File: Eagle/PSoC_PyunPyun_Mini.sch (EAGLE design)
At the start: 26 parts, among them IC1 NJM2732

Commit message: change Bord Design
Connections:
- net IDAC7: now also JP3.9; no longer JP3.8
- net IDAC8: now also JP3.8; no longer JP3.9
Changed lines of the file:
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@@
 <net name="IDAC8" class="0">
 <segment>
-<pinref part="JP3" gate="A" pin="9"/>
-<wire x1="101.6" y1="111.76" x2="114.3" y2="111.76" width="0.1524" layer="91"/>
-<wire x1="114.3" y1="111.76" x2="114.3" y2="86.36" width="0.1524" layer="91"/>
+<wire x1="114.3" y1="114.3" x2="114.3" y2="86.36" width="0.1524" layer="91"/>
 <wire x1="114.3" y1="86.36" x2="30.48" y2="86.36" width="0.1524" layer="91"/>
-<label x="106.68" y="111.76" size="1.778" layer="95"/>
 <pinref part="R5" gate="G$1" pin="1"/>
 <wire x1="30.48" y1="68.58" x2="35.56" y2="68.58" width="0.1524" layer="91"/>
@@
 <wire x1="30.48" y1="86.36" x2="30.48" y2="68.58" width="0.1524" layer="91"/>
 <junction x="30.48" y="68.58"/>
+<pinref part="JP3" gate="A" pin="8"/>
+<wire x1="101.6" y1="114.3" x2="114.3" y2="114.3" width="0.1524" layer="91"/>
+<label x="106.68" y="114.3" size="1.778" layer="95"/>
 </segment>
 </net>
@@
 <net name="IDAC7" class="0">
 <segment>
-<pinref part="JP3" gate="A" pin="8"/>
-<wire x1="101.6" y1="114.3" x2="114.3" y2="114.3" width="0.1524" layer="91"/>
-<label x="106.68" y="114.3" size="1.778" layer="95"/>
-</segment>
-</net>
+<pinref part="JP3" gate="A" pin="9"/>
+<wire x1="101.6" y1="111.76" x2="111.76" y2="111.76" width="0.1524" layer="91"/>
+<label x="106.68" y="111.76" size="1.778" layer="95"/>
+</segment>
+</net>

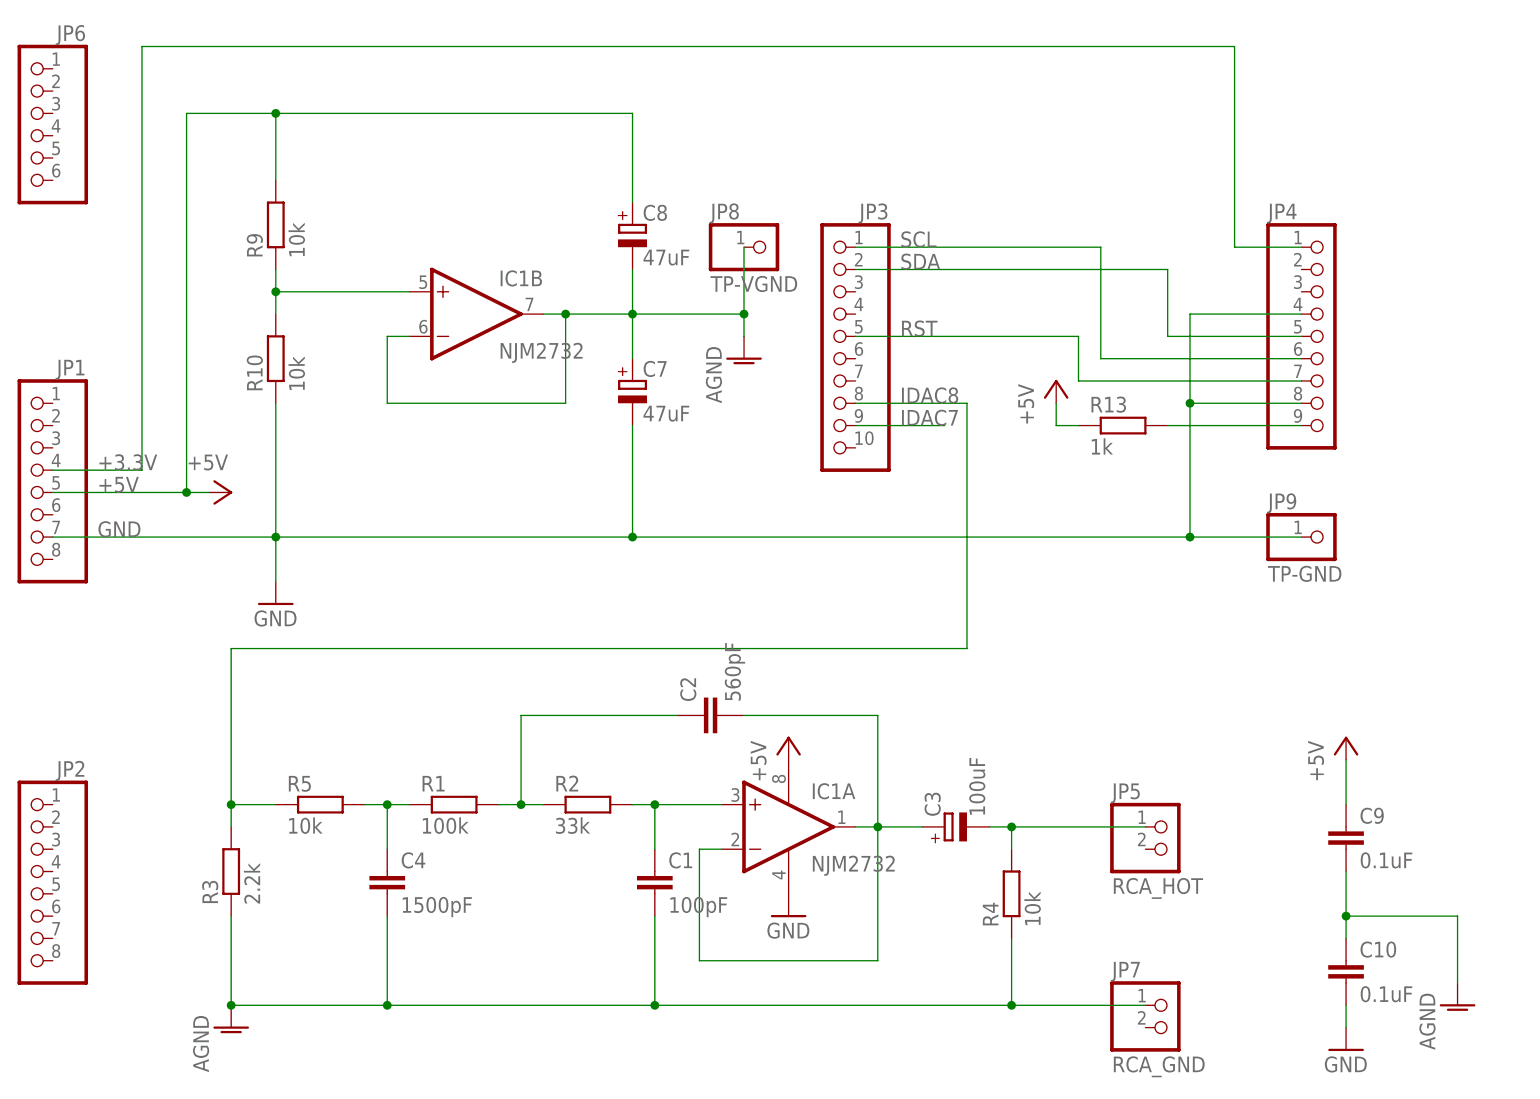
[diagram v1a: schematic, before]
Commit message: 回路図・基板図 RST信号に抵抗分圧を追加
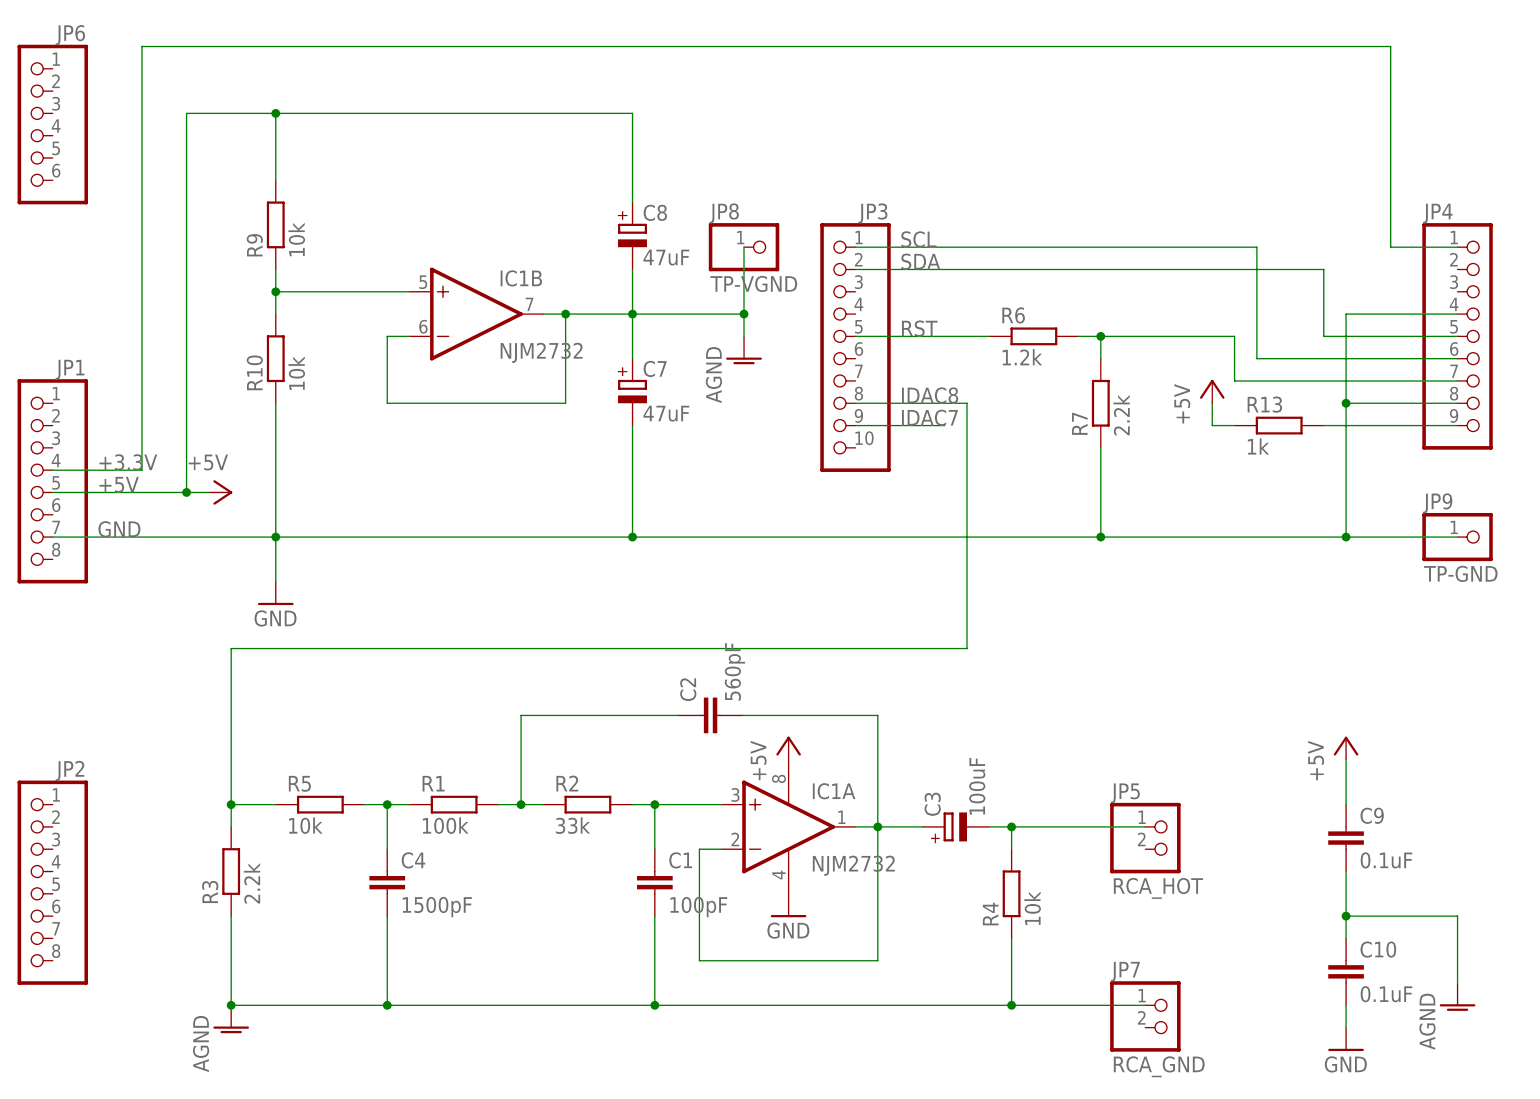
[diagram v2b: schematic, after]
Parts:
- added R6: 1.2k, rcl:R-EU_0207/7
- added R7: 2.2k, rcl:R-EU_0207/7
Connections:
- new net N$6: JP3.5, R6.1
- net GND: now also R7.1
- net RST: now also R6.2, R7.2; no longer JP3.5
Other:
- moved on the sheet: JP4, JP9, R13
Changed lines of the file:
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@@
 <setting verticaltext="up"/>
 </settings>
-<grid distance="0.1" unitdist="inch" unit="inch" style="lines" multiple="1" display="no" altdistance="0.01" altunitdist="inch" altunit="inch"/>
+<grid distance="0.1" unitdist="inch" unit="inch" style="dots" multiple="1" display="yes" altdistance="0.01" altunitdist="inch" altunit="inch"/>
 <layers>
 <layer number="1" name="Top" color="4" fill="1" visible="no" active="no"/>
@@
 <part name="JP9" library="pinhead" deviceset="PINHD-1X1" device="" value="TP-GND"/>
 <part name="JP4" library="pinhead" deviceset="PINHD-1X9" device=""/>
+<part name="R6" library="rcl" deviceset="R-EU_" device="0207/7" value="1.2k"/>
+<part name="R7" library="rcl" deviceset="R-EU_" device="0207/7" value="2.2k"/>
 </parts>
 <sheets>
@@
 <instance part="P+1" gate="1" x="30.48" y="104.14" rot="R270"/>
 <instance part="GND1" gate="1" x="35.56" y="91.44"/>
-<instance part="R13" gate="G$1" x="132.08" y="111.76"/>
-<instance part="P+2" gate="1" x="124.46" y="116.84"/>
+<instance part="R13" gate="G$1" x="149.86" y="111.76"/>
+<instance part="P+2" gate="1" x="142.24" y="116.84"/>
 <instance part="C9" gate="G$1" x="157.48" y="66.04"/>
 <instance part="C10" gate="G$1" x="157.48" y="50.8"/>
@@
 <instance part="C4" gate="G$1" x="48.26" y="60.96"/>
 <instance part="JP8" gate="G$1" x="91.44" y="132.08"/>
-<instance part="JP9" gate="G$1" x="154.94" y="99.06"/>
-<instance part="JP4" gate="A" x="154.94" y="121.92"/>
+<instance part="JP9" gate="G$1" x="172.72" y="99.06"/>
+<instance part="JP4" gate="A" x="172.72" y="121.92"/>
+<instance part="R6" gate="G$1" x="121.92" y="121.92"/>
+<instance part="R7" gate="G$1" x="129.54" y="114.3" rot="R90"/>
 </instances>
 <busses>
@@
 <junction x="35.56" y="99.06"/>
 <label x="15.24" y="99.06" size="1.778" layer="95"/>
-<wire x1="76.2" y1="99.06" x2="139.7" y2="99.06" width="0.1524" layer="91"/>
+<wire x1="76.2" y1="99.06" x2="129.54" y2="99.06" width="0.1524" layer="91"/>
 <junction x="76.2" y="99.06"/>
-<wire x1="139.7" y1="99.06" x2="139.7" y2="114.3" width="0.1524" layer="91"/>
-<wire x1="139.7" y1="114.3" x2="139.7" y2="124.46" width="0.1524" layer="91"/>
-<wire x1="139.7" y1="124.46" x2="152.4" y2="124.46" width="0.1524" layer="91"/>
+<wire x1="129.54" y1="99.06" x2="157.48" y2="99.06" width="0.1524" layer="91"/>
+<wire x1="157.48" y1="99.06" x2="157.48" y2="114.3" width="0.1524" layer="91"/>
+<wire x1="157.48" y1="114.3" x2="157.48" y2="124.46" width="0.1524" layer="91"/>
+<wire x1="157.48" y1="124.46" x2="170.18" y2="124.46" width="0.1524" layer="91"/>
 <pinref part="GND1" gate="1" pin="GND"/>
 <wire x1="35.56" y1="93.98" x2="35.56" y2="99.06" width="0.1524" layer="91"/>
 <pinref part="JP9" gate="G$1" pin="1"/>
-<wire x1="152.4" y1="99.06" x2="139.7" y2="99.06" width="0.1524" layer="91"/>
-<junction x="139.7" y="99.06"/>
+<wire x1="170.18" y1="99.06" x2="157.48" y2="99.06" width="0.1524" layer="91"/>
+<junction x="157.48" y="99.06"/>
 <pinref part="JP4" gate="A" pin="4"/>
 <pinref part="JP4" gate="A" pin="8"/>
-<wire x1="152.4" y1="114.3" x2="139.7" y2="114.3" width="0.1524" layer="91"/>
-<junction x="139.7" y="114.3"/>
+<wire x1="170.18" y1="114.3" x2="157.48" y2="114.3" width="0.1524" layer="91"/>
+<junction x="157.48" y="114.3"/>
+<pinref part="R7" gate="G$1" pin="1"/>
+<wire x1="129.54" y1="109.22" x2="129.54" y2="99.06" width="0.1524" layer="91"/>
+<junction x="129.54" y="99.06"/>
 </segment>
 <segment>
@@
 <pinref part="R13" gate="G$1" pin="1"/>
 <pinref part="P+2" gate="1" pin="+5V"/>
-<wire x1="127" y1="111.76" x2="124.46" y2="111.76" width="0.1524" layer="91"/>
-<wire x1="124.46" y1="111.76" x2="124.46" y2="114.3" width="0.1524" layer="91"/>
+<wire x1="144.78" y1="111.76" x2="142.24" y2="111.76" width="0.1524" layer="91"/>
+<wire x1="142.24" y1="111.76" x2="142.24" y2="114.3" width="0.1524" layer="91"/>
 </segment>
 <segment>
@@
 <wire x1="10.16" y1="106.68" x2="20.32" y2="106.68" width="0.1524" layer="91"/>
 <wire x1="20.32" y1="106.68" x2="20.32" y2="154.94" width="0.1524" layer="91"/>
-<wire x1="20.32" y1="154.94" x2="144.78" y2="154.94" width="0.1524" layer="91"/>
+<wire x1="20.32" y1="154.94" x2="162.56" y2="154.94" width="0.1524" layer="91"/>
 <label x="15.24" y="106.68" size="1.778" layer="95"/>
-<wire x1="144.78" y1="154.94" x2="144.78" y2="132.08" width="0.1524" layer="91"/>
+<wire x1="162.56" y1="154.94" x2="162.56" y2="132.08" width="0.1524" layer="91"/>
 <pinref part="JP4" gate="A" pin="1"/>
-<wire x1="144.78" y1="132.08" x2="152.4" y2="132.08" width="0.1524" layer="91"/>
+<wire x1="162.56" y1="132.08" x2="170.18" y2="132.08" width="0.1524" layer="91"/>
 </segment>
 </net>
 <net name="RST" class="0">
 <segment>
-<pinref part="JP3" gate="A" pin="5"/>
-<wire x1="101.6" y1="121.92" x2="127" y2="121.92" width="0.1524" layer="91"/>
 <label x="106.68" y="121.92" size="1.778" layer="95"/>
-<wire x1="127" y1="121.92" x2="127" y2="116.84" width="0.1524" layer="91"/>
+<wire x1="144.78" y1="121.92" x2="144.78" y2="116.84" width="0.1524" layer="91"/>
 <pinref part="JP4" gate="A" pin="7"/>
-<wire x1="127" y1="116.84" x2="152.4" y2="116.84" width="0.1524" layer="91"/>
+<wire x1="144.78" y1="116.84" x2="170.18" y2="116.84" width="0.1524" layer="91"/>
+<pinref part="R6" gate="G$1" pin="2"/>
+<wire x1="127" y1="121.92" x2="129.54" y2="121.92" width="0.1524" layer="91"/>
+<pinref part="R7" gate="G$1" pin="2"/>
+<wire x1="129.54" y1="121.92" x2="144.78" y2="121.92" width="0.1524" layer="91"/>
+<wire x1="129.54" y1="119.38" x2="129.54" y2="121.92" width="0.1524" layer="91"/>
+<junction x="129.54" y="121.92"/>
 </segment>
 </net>
@@
 <segment>
 <pinref part="JP3" gate="A" pin="1"/>
-<wire x1="101.6" y1="132.08" x2="129.54" y2="132.08" width="0.1524" layer="91"/>
+<wire x1="101.6" y1="132.08" x2="147.32" y2="132.08" width="0.1524" layer="91"/>
 <label x="106.68" y="132.08" size="1.778" layer="95"/>
 <pinref part="JP4" gate="A" pin="6"/>
-<wire x1="152.4" y1="119.38" x2="129.54" y2="119.38" width="0.1524" layer="91"/>
-<wire x1="129.54" y1="119.38" x2="129.54" y2="132.08" width="0.1524" layer="91"/>
+<wire x1="170.18" y1="119.38" x2="147.32" y2="119.38" width="0.1524" layer="91"/>
+<wire x1="147.32" y1="119.38" x2="147.32" y2="132.08" width="0.1524" layer="91"/>
 </segment>
 </net>
@@
 <segment>
 <pinref part="JP3" gate="A" pin="2"/>
-<wire x1="101.6" y1="129.54" x2="137.16" y2="129.54" width="0.1524" layer="91"/>
+<wire x1="101.6" y1="129.54" x2="154.94" y2="129.54" width="0.1524" layer="91"/>
 <label x="106.68" y="129.54" size="1.778" layer="95"/>
 <pinref part="JP4" gate="A" pin="5"/>
-<wire x1="152.4" y1="121.92" x2="137.16" y2="121.92" width="0.1524" layer="91"/>
-<wire x1="137.16" y1="121.92" x2="137.16" y2="129.54" width="0.1524" layer="91"/>
+<wire x1="170.18" y1="121.92" x2="154.94" y2="121.92" width="0.1524" layer="91"/>
+<wire x1="154.94" y1="121.92" x2="154.94" y2="129.54" width="0.1524" layer="91"/>
 </segment>
 </net>
@@
 <segment>
 <pinref part="R13" gate="G$1" pin="2"/>
-<wire x1="137.16" y1="111.76" x2="152.4" y2="111.76" width="0.1524" layer="91"/>
+<wire x1="154.94" y1="111.76" x2="170.18" y2="111.76" width="0.1524" layer="91"/>
 <pinref part="JP4" gate="A" pin="9"/>
 </segment>
@@
 </segment>
 </net>
+<net name="N$6" class="0">
+<segment>
+<pinref part="JP3" gate="A" pin="5"/>
+<pinref part="R6" gate="G$1" pin="1"/>
+<wire x1="101.6" y1="121.92" x2="116.84" y2="121.92" width="0.1524" layer="91"/>
+</segment>
+</net>
